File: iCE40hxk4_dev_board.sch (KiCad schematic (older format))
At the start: 0 parts

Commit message: No more DRC errors :)
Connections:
- wire segments 64 -> 67
- no-connect marks 18 -> 55
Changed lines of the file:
@@
 	1    0    0    -1
 $EndComp
-Wire Wire Line
-	625  2525 925  2525
-Wire Wire Line
-	775  2675 925  2675
-Wire Wire Line
-	2575 1975 3825 1975
-Wire Wire Line
-	6075 3325 5525 3325
-Wire Wire Line
-	2575 2125 3825 2125
-Wire Wire Line
-	2775 1975 2775 1875
-Connection ~ 2775 1975
-Wire Wire Line
-	3825 4325 3675 4325
-Wire Wire Line
-	5875 6275 5525 6275
 $Comp
 L GND #PWR04
@@
 	1    0    0    -1
 $EndComp
-Wire Wire Line
-	5775 6975 5975 6975
-Wire Wire Line
-	3825 4575 2575 4575
-Wire Wire Line
-	3825 4675 2575 4675
-Wire Wire Line
-	2575 4775 3825 4775
-Wire Wire Line
-	3825 4875 2575 4875
-Wire Wire Line
-	2575 4975 3825 4975
-Wire Wire Line
-	3825 5075 2575 5075
-Wire Wire Line
-	2575 5175 3825 5175
-Wire Wire Line
-	3825 5275 2575 5275
-Wire Wire Line
-	2575 5425 3825 5425
-Wire Wire Line
-	2575 5525 3825 5525
-Wire Wire Line
-	2575 5625 3825 5625
-Wire Wire Line
-	2575 5725 3825 5725
-Wire Wire Line
-	2575 5825 3825 5825
-Wire Wire Line
-	2575 2425 3825 2425
-Wire Wire Line
-	2575 2525 3825 2525
-Wire Wire Line
-	2575 2625 3825 2625
-Wire Wire Line
-	2575 2775 3825 2775
-Wire Wire Line
-	2575 2875 3825 2875
-Wire Wire Line
-	2575 2975 3825 2975
 $Sheet
 S 6525 3975 1750 2450
@@
 F31 "+5V" I L 6525 4025 60
 $EndSheet
-Wire Wire Line
-	5525 4725 6525 4725
-Wire Wire Line
-	6525 4825 5525 4825
-Wire Wire Line
-	5525 4925 6525 4925
-Wire Wire Line
-	6525 5025 5525 5025
-Wire Wire Line
-	5525 5125 6525 5125
-Wire Wire Line
-	6525 5225 5525 5225
-Wire Wire Line
-	5525 5325 6525 5325
-Wire Wire Line
-	5525 5875 6525 5875
-Wire Wire Line
-	5525 5775 6525 5775
-Wire Wire Line
-	8275 4375 8375 4375
-Wire Wire Line
-	8275 4475 8375 4475
-Wire Wire Line
-	8275 4575 8375 4575
-Wire Wire Line
-	8275 4675 8375 4675
-Wire Wire Line
-	8275 4775 8375 4775
-Wire Wire Line
-	8275 4875 8375 4875
-Wire Wire Line
-	8275 4975 8375 4975
-Wire Wire Line
-	8275 5075 8375 5075
-Wire Wire Line
-	8275 5175 8375 5175
-Wire Wire Line
-	8275 5275 8375 5275
-Wire Wire Line
-	8275 5375 8375 5375
-Wire Wire Line
-	8275 5475 8375 5475
-Wire Wire Line
-	8275 5575 8375 5575
-Wire Wire Line
-	8275 5675 8375 5675
-Wire Wire Line
-	8275 5775 8375 5775
-Wire Wire Line
-	8275 5875 8375 5875
-Wire Wire Line
-	8275 5975 8375 5975
-Wire Wire Line
-	8275 6075 8375 6075
 NoConn ~ 8375 4375
 NoConn ~ 8375 4475
@@
 	1    0    0    -1
 $EndComp
-Wire Wire Line
-	6525 4325 6275 4325
-Wire Wire Line
-	6275 4325 6275 4225
 $Comp
 L GNDD #PWR010
@@
 	1    0    0    -1
 $EndComp
-Wire Wire Line
-	8275 6325 8475 6325
-Wire Wire Line
-	2575 4025 3825 4025
 $Comp
 L +5V #PWR011
@@
 	1    0    0    -1
 $EndComp
-Wire Wire Line
-	6275 4025 6525 4025
-Wire Wire Line
-	6275 3925 6275 4025
-Wire Wire Line
-	2675 3975 2675 4025
-Connection ~ 2675 4025
 $Sheet
 S 3825 3875 1700 2550
@@
 F26 "A5" I R 5525 5875 60
 $EndSheet
+$Comp
+L GNDA #PWR013
+U 1 1 596F148C
+P 6400 3550
+F 0 "#PWR013" H 6400 3300 50  0001 C CNN
+F 1 "GNDA" H 6400 3400 50  0000 C CNN
+F 2 "" H 6400 3550 50  0001 C CNN
+F 3 "" H 6400 3550 50  0001 C CNN
+	1    6400 3550
+	1    0    0    -1
+$EndComp
+$Comp
+L GNDD #PWR014
+U 1 1 596F17BC
+P 8650 3550
+F 0 "#PWR014" H 8650 3300 50  0001 C CNN
+F 1 "GNDD" H 8650 3400 50  0000 C CNN
+F 2 "" H 8650 3550 50  0001 C CNN
+F 3 "" H 8650 3550 50  0001 C CNN
+	1    8650 3550
+	-1   0    0    -1
+$EndComp
+$Comp
+L +3.3V #PWR015
+U 1 1 59674AAB
+P 6300 750
+F 0 "#PWR015" H 6300 600 50  0001 C CNN
+F 1 "+3.3V" H 6300 890 50  0000 C CNN
+F 2 "" H 6300 750 50  0001 C CNN
+F 3 "" H 6300 750 50  0001 C CNN
+	1    6300 750
+	1    0    0    -1
+$EndComp
+$Comp
+L +5V #PWR016
+U 1 1 59678316
+P 8700 725
+F 0 "#PWR016" H 8700 575 50  0001 C CNN
+F 1 "+5V" H 8700 865 50  0000 C CNN
+F 2 "" H 8700 725 50  0001 C CNN
+F 3 "" H 8700 725 50  0001 C CNN
+	1    8700 725
+	1    0    0    -1
+$EndComp
+Wire Wire Line
+	625  2525 925  2525
+Wire Wire Line
+	775  2675 925  2675
+Wire Wire Line
+	2575 1975 3825 1975
+Wire Wire Line
+	6075 3325 5525 3325
+Wire Wire Line
+	2575 2125 3825 2125
+Wire Wire Line
+	2775 1975 2775 1875
+Connection ~ 2775 1975
+Wire Wire Line
+	3825 4325 3675 4325
+Wire Wire Line
+	5875 6275 5525 6275
+Wire Wire Line
+	5575 6975 5975 6975
+Wire Wire Line
+	3825 4575 2575 4575
+Wire Wire Line
+	3825 4675 2575 4675
+Wire Wire Line
+	2575 4775 3825 4775
+Wire Wire Line
+	3825 4875 2575 4875
+Wire Wire Line
+	2575 4975 3825 4975
+Wire Wire Line
+	3825 5075 2575 5075
+Wire Wire Line
+	2575 5175 3825 5175
+Wire Wire Line
+	3825 5275 2575 5275
+Wire Wire Line
+	2575 5425 3825 5425
+Wire Wire Line
+	2575 5525 3825 5525
+Wire Wire Line
+	2575 5625 3825 5625
+Wire Wire Line
+	2575 5725 3825 5725
+Wire Wire Line
+	2575 5825 3825 5825
+Wire Wire Line
+	2575 2425 3825 2425
+Wire Wire Line
+	2575 2525 3825 2525
+Wire Wire Line
+	2575 2625 3825 2625
+Wire Wire Line
+	2575 2775 3825 2775
+Wire Wire Line
+	2575 2875 3825 2875
+Wire Wire Line
+	2575 2975 3825 2975
+Wire Wire Line
+	5525 4725 6525 4725
+Wire Wire Line
+	6525 4825 5525 4825
+Wire Wire Line
+	5525 4925 6525 4925
+Wire Wire Line
+	6525 5025 5525 5025
+Wire Wire Line
+	5525 5125 6525 5125
+Wire Wire Line
+	6525 5225 5525 5225
+Wire Wire Line
+	5525 5325 6525 5325
+Wire Wire Line
+	5525 5875 6525 5875
+Wire Wire Line
+	5525 5775 6525 5775
+Wire Wire Line
+	8275 4375 8375 4375
+Wire Wire Line
+	8275 4475 8375 4475
+Wire Wire Line
+	8275 4575 8375 4575
+Wire Wire Line
+	8275 4675 8375 4675
+Wire Wire Line
+	8275 4775 8375 4775
+Wire Wire Line
+	8275 4875 8375 4875
+Wire Wire Line
+	8275 4975 8375 4975
+Wire Wire Line
+	8275 5075 8375 5075
+Wire Wire Line
+	8275 5175 8375 5175
+Wire Wire Line
+	8275 5275 8375 5275
+Wire Wire Line
+	8275 5375 8375 5375
+Wire Wire Line
+	8275 5475 8375 5475
+Wire Wire Line
+	8275 5575 8375 5575
+Wire Wire Line
+	8275 5675 8375 5675
+Wire Wire Line
+	8275 5775 8375 5775
+Wire Wire Line
+	8275 5875 8375 5875
+Wire Wire Line
+	8275 5975 8375 5975
+Wire Wire Line
+	8275 6075 8375 6075
+Wire Wire Line
+	6525 4325 6275 4325
+Wire Wire Line
+	6275 4325 6275 4225
+Wire Wire Line
+	8275 6325 8475 6325
+Wire Wire Line
+	2575 4025 3825 4025
+Wire Wire Line
+	6275 4025 6525 4025
+Wire Wire Line
+	6275 3925 6275 4025
+Wire Wire Line
+	2675 3975 2675 4025
+Connection ~ 2675 4025
+Wire Wire Line
+	6400 3550 6525 3550
+Wire Wire Line
+	8525 3550 8650 3550
+Wire Wire Line
+	6525 750  6300 750
+Wire Wire Line
+	8525 750  8700 750
+Wire Wire Line
+	8700 750  8700 725
+$Comp
+L GNDA #PWR017
+U 1 1 596A4A64
+P 5575 6975
+F 0 "#PWR017" H 5575 6725 50  0001 C CNN
+F 1 "GNDA" H 5575 6825 50  0000 C CNN
+F 2 "" H 5575 6975 50  0001 C CNN
+F 3 "" H 5575 6975 50  0001 C CNN
+	1    5575 6975
+	1    0    0    -1
+$EndComp
+Connection ~ 5775 6975
+NoConn ~ 6525 1100
+NoConn ~ 6525 1200
+NoConn ~ 6525 1300
+NoConn ~ 6525 1400
+NoConn ~ 6525 1575
+NoConn ~ 6525 1750
+NoConn ~ 6525 1850
+NoConn ~ 6525 1950
+NoConn ~ 6525 2050
+NoConn ~ 6525 2250
+NoConn ~ 6525 2350
+NoConn ~ 6525 2450
+NoConn ~ 6525 2550
+NoConn ~ 6525 2650
+NoConn ~ 6525 2750
+NoConn ~ 6525 2850
+NoConn ~ 6525 2950
+NoConn ~ 6525 3050
+NoConn ~ 8525 2250
+NoConn ~ 8525 2350
+NoConn ~ 8525 2450
+NoConn ~ 8525 2550
+NoConn ~ 8525 2650
+NoConn ~ 8525 2750
+NoConn ~ 8525 2850
+NoConn ~ 8525 2950
+NoConn ~ 8525 3050
+NoConn ~ 8525 1750
+NoConn ~ 8525 1850
+NoConn ~ 8525 1950
+NoConn ~ 8525 2050
+NoConn ~ 8525 1575
+NoConn ~ 8525 1100
+NoConn ~ 8525 1200
+NoConn ~ 8525 1300
+NoConn ~ 8525 1400
+NoConn ~ 8525 1100
 $Sheet
 S 6525 650  2000 3050
@@
 F46 "SCL_OFF" I L 6525 3275 60
 $EndSheet
-$Comp
-L GNDA #PWR013
-U 1 1 596F148C
-P 6400 3550
-F 0 "#PWR013" H 6400 3300 50  0001 C CNN
-F 1 "GNDA" H 6400 3400 50  0000 C CNN
-F 2 "" H 6400 3550 50  0001 C CNN
-F 3 "" H 6400 3550 50  0001 C CNN
-	1    6400 3550
-	1    0    0    -1
-$EndComp
-$Comp
-L GNDD #PWR014
-U 1 1 596F17BC
-P 8650 3550
-F 0 "#PWR014" H 8650 3300 50  0001 C CNN
-F 1 "GNDD" H 8650 3400 50  0000 C CNN
-F 2 "" H 8650 3550 50  0001 C CNN
-F 3 "" H 8650 3550 50  0001 C CNN
-	1    8650 3550
-	-1   0    0    -1
-$EndComp
-Wire Wire Line
-	6400 3550 6525 3550
-Wire Wire Line
-	8525 3550 8650 3550
 $EndSCHEMATC

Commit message: Assignement of FPGA pins for analog stage control
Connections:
- wire segments 67 -> 83
- no-connect marks 55 -> 3

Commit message: Startin routing the analog side of the force
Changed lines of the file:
@@
 F20 "CHB_GAIN_SEL_2" I L 8525 3425 60
 F21 "CHB_GAIN_EN" I L 8525 3525 60
-F22 "CHA_D0" O L 8525 4450 60
-F23 "CHA_D1" O L 8525 4550 60
-F24 "CHA_D2" O L 8525 4650 60
-F25 "CHA_D3" O L 8525 4750 60
-F26 "CHA_D4" O L 8525 4850 60
-F27 "CHA_D5" O L 8525 4950 60
-F28 "CHA_D6" O L 8525 5050 60
-F29 "CHA_D7" O L 8525 5150 60
-F30 "CHB_D0" O L 8525 5250 60
-F31 "CHB_D1" O L 8525 5350 60
-F32 "CHB_D2" O L 8525 5450 60
-F33 "CHB_D3" O L 8525 5550 60
-F34 "CHB_D4" O L 8525 5650 60
-F35 "CHB_D5" O L 8525 5750 60
-F36 "CHB_D6" O L 8525 5850 60
-F37 "CHB_D7" O L 8525 5950 60
+F22 "CHA_D0" O L 8525 5950 60
+F23 "CHA_D1" O L 8525 5850 60
+F24 "CHA_D2" O L 8525 5750 60
+F25 "CHA_D3" O L 8525 5650 60
+F26 "CHA_D4" O L 8525 5550 60
+F27 "CHA_D5" O L 8525 5450 60
+F28 "CHA_D6" O L 8525 5350 60
+F29 "CHA_D7" O L 8525 5250 60
+F30 "CHB_D0" O L 8525 5150 60
+F31 "CHB_D1" O L 8525 5050 60
+F32 "CHB_D2" O L 8525 4950 60
+F33 "CHB_D3" O L 8525 4850 60
+F34 "CHB_D4" O L 8525 4750 60
+F35 "CHB_D5" O L 8525 4650 60
+F36 "CHB_D6" O L 8525 4550 60
+F37 "CHB_D7" O L 8525 4450 60
 F38 "CHA_ADC_OE" I R 10450 3850 60
 F39 "CHB_ADC_OE" I R 10450 3950 60

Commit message: Almost finish
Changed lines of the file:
@@
 F0 "RIGHT_TOP_BANKs" 79
 F1 "RIGHT_TOP_BANKs.sch" 79
-F2 "IOT_168" B R 8100 2925 60
-F3 "IOT_169" B R 8100 3125 60
-F4 "IOT_170" B R 8100 3225 60
-F5 "IOT_171" B R 8100 3325 60
-F6 "IOT_172" B R 8100 3425 60
-F7 "IOT_173" B R 8100 3525 60
+F2 "IOT_168" B R 8100 3225 60
+F3 "IOT_169" B R 8100 3525 60
+F4 "IOT_170" B R 8100 3025 60
+F5 "IOT_171" B R 8100 2925 60
+F6 "IOT_172" B R 8100 2825 60
+F7 "IOT_173" B R 8100 3125 60
 F8 "IOT_174" B R 8100 3625 60
 F9 "ADC_0" B R 8100 4450 60
@@
 F30 "IOT_177" B R 8100 3725 60
 F31 "IOT_178" B R 8100 3825 60
-F32 "IOT_144" B R 8100 1925 60
-F33 "IOT_146" B R 8100 2025 60
-F34 "IOT_147" B R 8100 2125 60
-F35 "IOT_148" B R 8100 2225 60
-F36 "IOT_152" B R 8100 2325 60
-F37 "IOT_160" B R 8100 2425 60
-F38 "IOT_161" B R 8100 2525 60
-F39 "IOT_164" B R 8100 2625 60
-F40 "IOT_165" B R 8100 2725 60
-F41 "IOT_166" B R 8100 2825 60
-F42 "IOT_167" B R 8100 3025 60
+F32 "IOT_144" B R 8100 2725 60
+F33 "IOT_146" B R 8100 2225 60
+F34 "IOT_147" B R 8100 2325 60
+F35 "IOT_148" B R 8100 2425 60
+F36 "IOT_152" B R 8100 2525 60
+F37 "IOT_160" B R 8100 1825 60
+F38 "IOT_161" B R 8100 1925 60
+F39 "IOT_164" B R 8100 2025 60
+F40 "IOT_165" B R 8100 2125 60
+F41 "IOT_166" B R 8100 3425 60
+F42 "IOT_167" B R 8100 3325 60
 F43 "IOT_139" B R 8100 1625 60
-F44 "IOT_140" B R 8100 1825 60
+F44 "IOT_140" B R 8100 2625 60
 $EndSheet
 Wire Wire Line

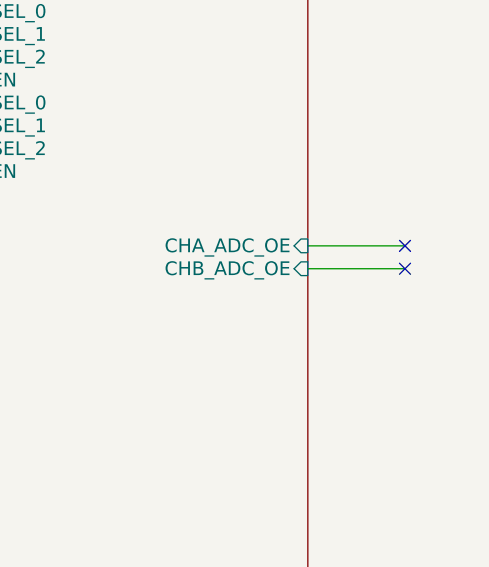
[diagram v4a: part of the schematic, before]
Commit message: Changed part number of DAC (different dir). Connected ADC_OE to GND.
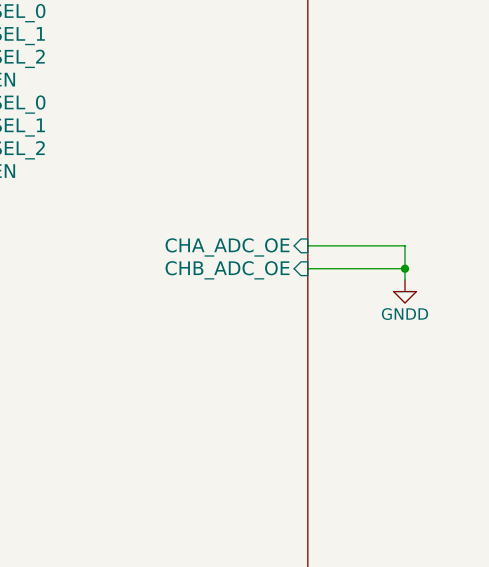
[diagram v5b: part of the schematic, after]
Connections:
- wire segments 83 -> 84
- no-connect marks 3 -> 1
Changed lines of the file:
@@
 Wire Wire Line
 	10450 1925 10800 1925
-NoConn ~ 10875 3850
-NoConn ~ 10875 3950
+$Comp
+L GNDD #PWR?
+U 1 1 59938834
+P 10875 4000
+F 0 "#PWR?" H 10875 3750 50  0001 C CNN
+F 1 "GNDD" H 10875 3850 50  0000 C CNN
+F 2 "" H 10875 4000 50  0001 C CNN
+F 3 "" H 10875 4000 50  0001 C CNN
+	1    10875 4000
+	1    0    0    -1
+$EndComp
+Wire Wire Line
+	10875 3850 10875 4000
+Connection ~ 10875 3950
 $EndSCHEMATC

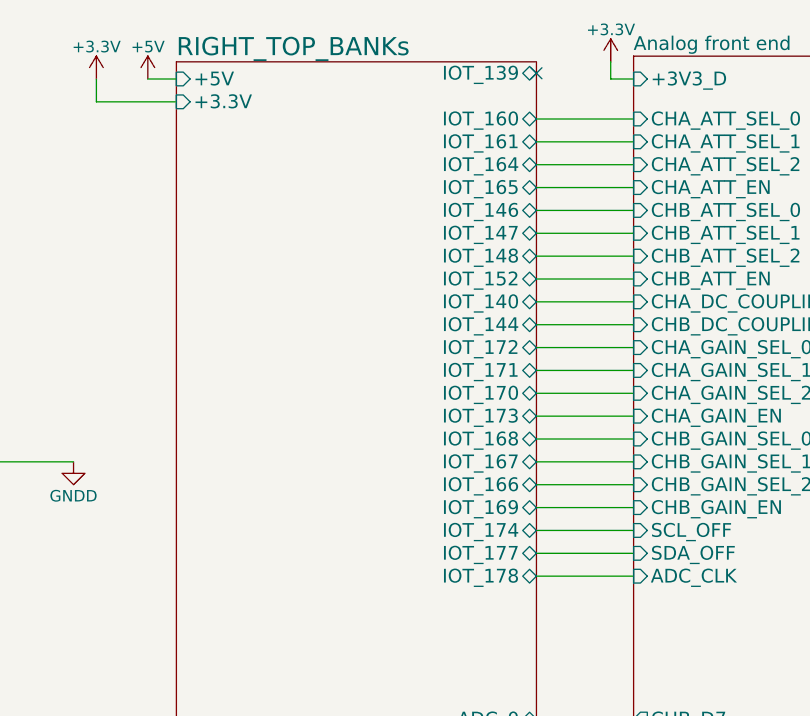
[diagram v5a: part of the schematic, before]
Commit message: Added reset button. Delated unused fpga analog control connections. Added this connections to the expansion connector
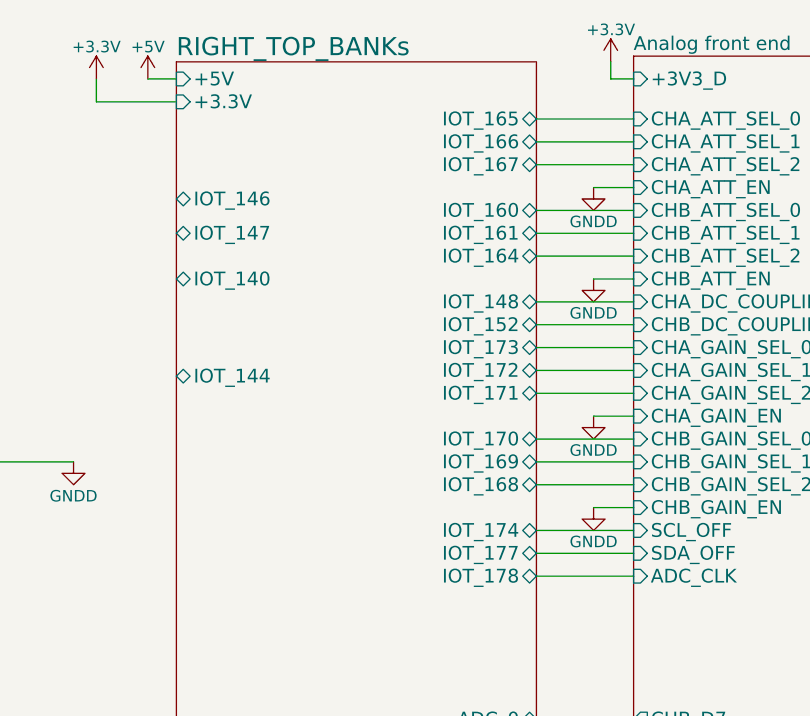
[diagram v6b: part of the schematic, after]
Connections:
- no-connect marks 1 -> 0
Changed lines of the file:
@@
 LIBS:voltage-references
 LIBS:voltage-regulators
+LIBS:switches
 LIBS:iCE40hxk4_dev_board-cache
 EELAYER 25 0
@@
 F0 "RIGHT_TOP_BANKs" 79
 F1 "RIGHT_TOP_BANKs.sch" 79
-F2 "IOT_168" B R 8100 3225 60
-F3 "IOT_169" B R 8100 3525 60
-F4 "IOT_170" B R 8100 3025 60
-F5 "IOT_171" B R 8100 2925 60
-F6 "IOT_172" B R 8100 2825 60
-F7 "IOT_173" B R 8100 3125 60
+F2 "IOT_168" B R 8100 3425 60
+F3 "IOT_169" B R 8100 3325 60
+F4 "IOT_170" B R 8100 3225 60
+F5 "IOT_171" B R 8100 3025 60
+F6 "IOT_172" B R 8100 2925 60
+F7 "IOT_173" B R 8100 2825 60
 F8 "IOT_174" B R 8100 3625 60
 F9 "ADC_0" B R 8100 4450 60
@@
 F30 "IOT_177" B R 8100 3725 60
 F31 "IOT_178" B R 8100 3825 60
-F32 "IOT_144" B R 8100 2725 60
-F33 "IOT_146" B R 8100 2225 60
-F34 "IOT_147" B R 8100 2325 60
-F35 "IOT_148" B R 8100 2425 60
-F36 "IOT_152" B R 8100 2525 60
-F37 "IOT_160" B R 8100 1825 60
-F38 "IOT_161" B R 8100 1925 60
-F39 "IOT_164" B R 8100 2025 60
-F40 "IOT_165" B R 8100 2125 60
-F41 "IOT_166" B R 8100 3425 60
-F42 "IOT_167" B R 8100 3325 60
-F43 "IOT_139" B R 8100 1625 60
-F44 "IOT_140" B R 8100 2625 60
+F32 "IOT_144" B L 6525 2950 60
+F33 "IOT_146" B L 6525 2175 60
+F34 "IOT_147" B L 6525 2325 60
+F35 "IOT_148" B R 8100 2625 60
+F36 "IOT_152" B R 8100 2725 60
+F37 "IOT_160" B R 8100 2225 60
+F38 "IOT_161" B R 8100 2325 60
+F39 "IOT_164" B R 8100 2425 60
+F40 "IOT_165" B R 8100 1825 60
+F41 "IOT_166" B R 8100 1925 60
+F42 "IOT_167" B R 8100 2025 60
+F44 "IOT_140" B L 6525 2525 60
 $EndSheet
 Wire Wire Line
@@
 	8100 2025 8525 2025
 Wire Wire Line
-	8100 2125 8525 2125
-Wire Wire Line
 	8100 2225 8525 2225
 Wire Wire Line
@@
 	8100 2425 8525 2425
 Wire Wire Line
-	8100 2525 8525 2525
-Wire Wire Line
 	8100 2625 8525 2625
 Wire Wire Line
@@
 	8100 3025 8525 3025
 Wire Wire Line
-	8100 3125 8525 3125
-Wire Wire Line
 	8100 3225 8525 3225
 Wire Wire Line
@@
 Wire Wire Line
 	8100 3425 8525 3425
-Wire Wire Line
-	8100 3525 8525 3525
 Wire Wire Line
 	8100 3625 8525 3625
@@
 	1    0    0    -1
 $EndComp
-NoConn ~ 8100 1625
 Wire Wire Line
 	6525 5900 5525 5900
@@
 	10450 1925 10800 1925
 $Comp
-L GNDD #PWR?
+L GNDD #PWR017
 U 1 1 59938834
 P 10875 4000
-F 0 "#PWR?" H 10875 3750 50  0001 C CNN
+F 0 "#PWR017" H 10875 3750 50  0001 C CNN
 F 1 "GNDD" H 10875 3850 50  0000 C CNN
 F 2 "" H 10875 4000 50  0001 C CNN
@@
 	10875 3850 10875 4000
 Connection ~ 10875 3950
+$Comp
+L GNDD #PWR018
+U 1 1 59940669
+P 8350 2125
+F 0 "#PWR018" H 8350 1875 50  0001 C CNN
+F 1 "GNDD" H 8350 1975 50  0000 C CNN
+F 2 "" H 8350 2125 50  0001 C CNN
+F 3 "" H 8350 2125 50  0001 C CNN
+	1    8350 2125
+	-1   0    0    -1
+$EndComp
+$Comp
+L GNDD #PWR019
+U 1 1 599409AA
+P 8350 2525
+F 0 "#PWR019" H 8350 2275 50  0001 C CNN
+F 1 "GNDD" H 8350 2375 50  0000 C CNN
+F 2 "" H 8350 2525 50  0001 C CNN
+F 3 "" H 8350 2525 50  0001 C CNN
+	1    8350 2525
+	-1   0    0    -1
+$EndComp
+$Comp
+L GNDD #PWR020
+U 1 1 59940CEB
+P 8350 3125
+F 0 "#PWR020" H 8350 2875 50  0001 C CNN
+F 1 "GNDD" H 8350 2975 50  0000 C CNN
+F 2 "" H 8350 3125 50  0001 C CNN
+F 3 "" H 8350 3125 50  0001 C CNN
+	1    8350 3125
+	-1   0    0    -1
+$EndComp
+Wire Wire Line
+	8350 2125 8525 2125
+Wire Wire Line
+	8350 2525 8525 2525
+Wire Wire Line
+	8350 3125 8525 3125
+$Comp
+L GNDD #PWR021
+U 1 1 5994102C
+P 8350 3525
+F 0 "#PWR021" H 8350 3275 50  0001 C CNN
+F 1 "GNDD" H 8350 3375 50  0000 C CNN
+F 2 "" H 8350 3525 50  0001 C CNN
+F 3 "" H 8350 3525 50  0001 C CNN
+	1    8350 3525
+	-1   0    0    -1
+$EndComp
+Wire Wire Line
+	8350 3525 8525 3525
 $EndSCHEMATC
